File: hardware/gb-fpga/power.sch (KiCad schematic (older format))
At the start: 1 part, among them U1 xc7s25ftgb196

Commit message: Add GND net
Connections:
- net labels added: GND
- wire segments 0 -> 2
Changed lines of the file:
@@
 	1    0    0    -1
 $EndComp
+$Comp
+L power:GND #PWR0102
+U 1 1 60D21807
+P 5500 3700
+F 0 "#PWR0102" H 5500 3450 50  0001 C CNN
+F 1 "GND" H 5505 3527 50  0000 C CNN
+F 2 "" H 5500 3700 50  0001 C CNN
+F 3 "" H 5500 3700 50  0001 C CNN
+	1    5500 3700
+	1    0    0    -1
+$EndComp
+Wire Wire Line
+	6050 3100 5500 3100
+Wire Wire Line
+	5500 3100 5500 3700
 $EndSCHEMATC

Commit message: Connect flash config circuit
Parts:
- removed U1: xc7s25ftgb196, Package_BGA:Xilinx_FTGB196, symbol xilinx7:xc7s25ftgb196
- added U1: xc7s25ftgb196, Package_BGA:Xilinx_FTGB196, symbol gb-fpga:xc7s25ftgb196
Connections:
- net labels added: +1V0, +1V8, +3V3
- wire segments 2 -> 79

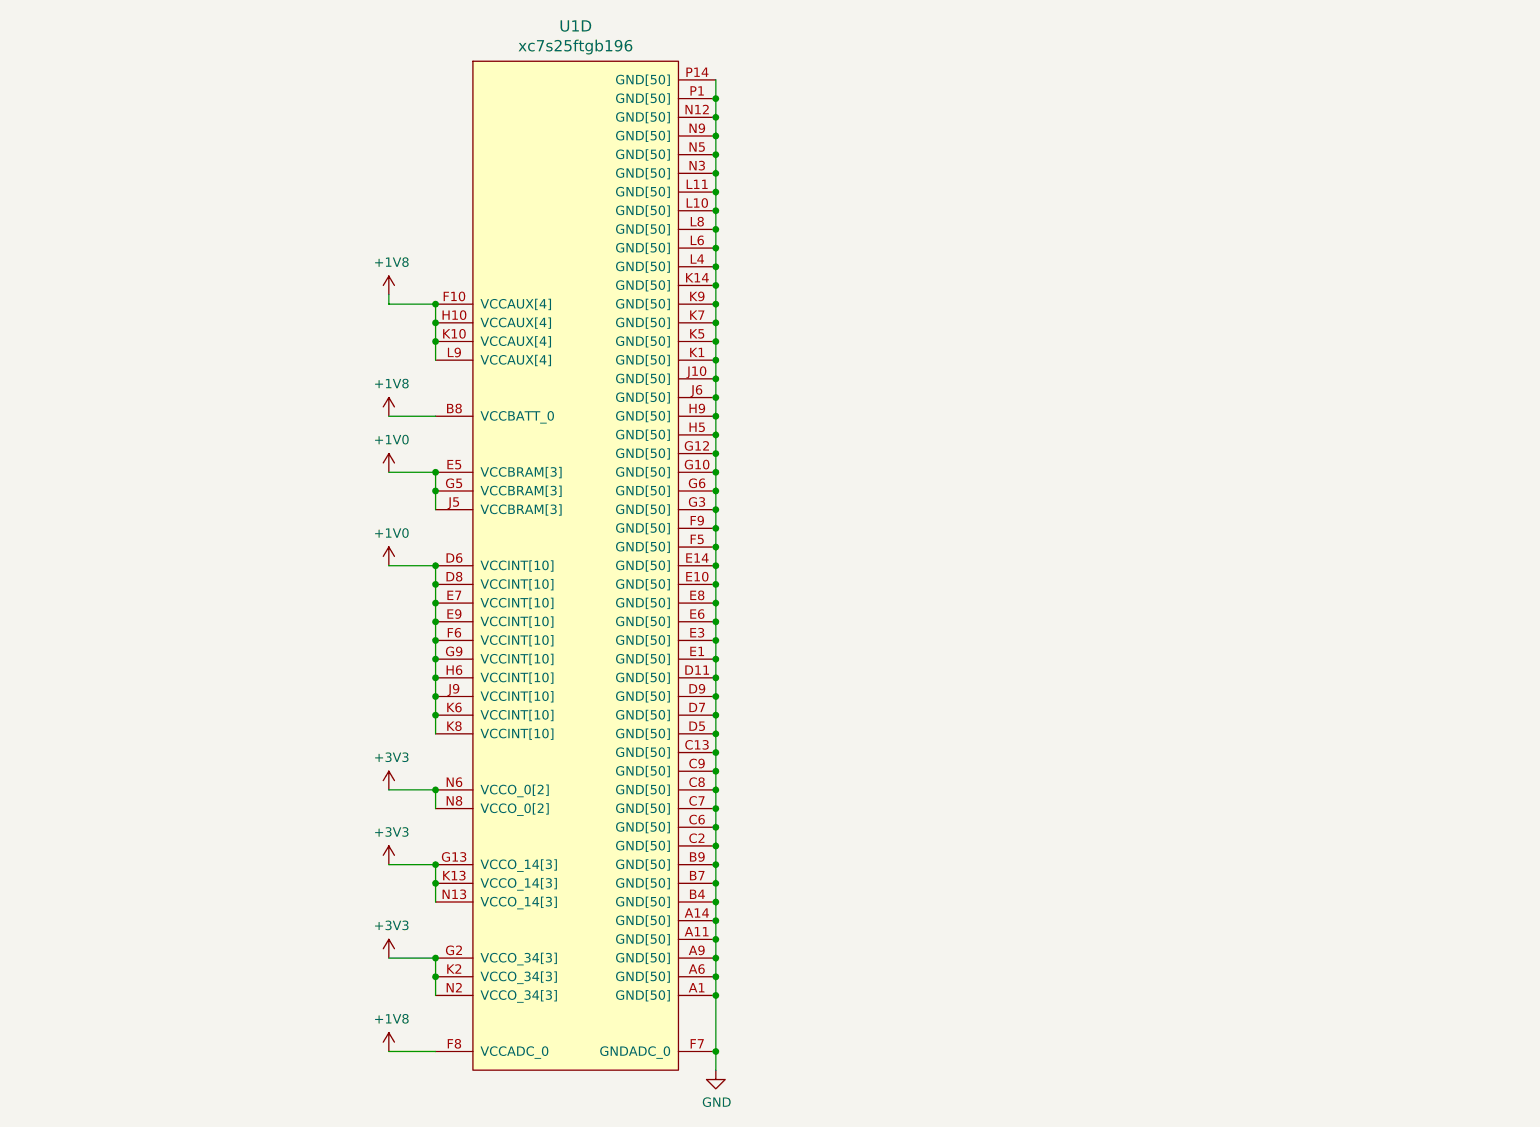
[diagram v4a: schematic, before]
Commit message: Add LTC3555
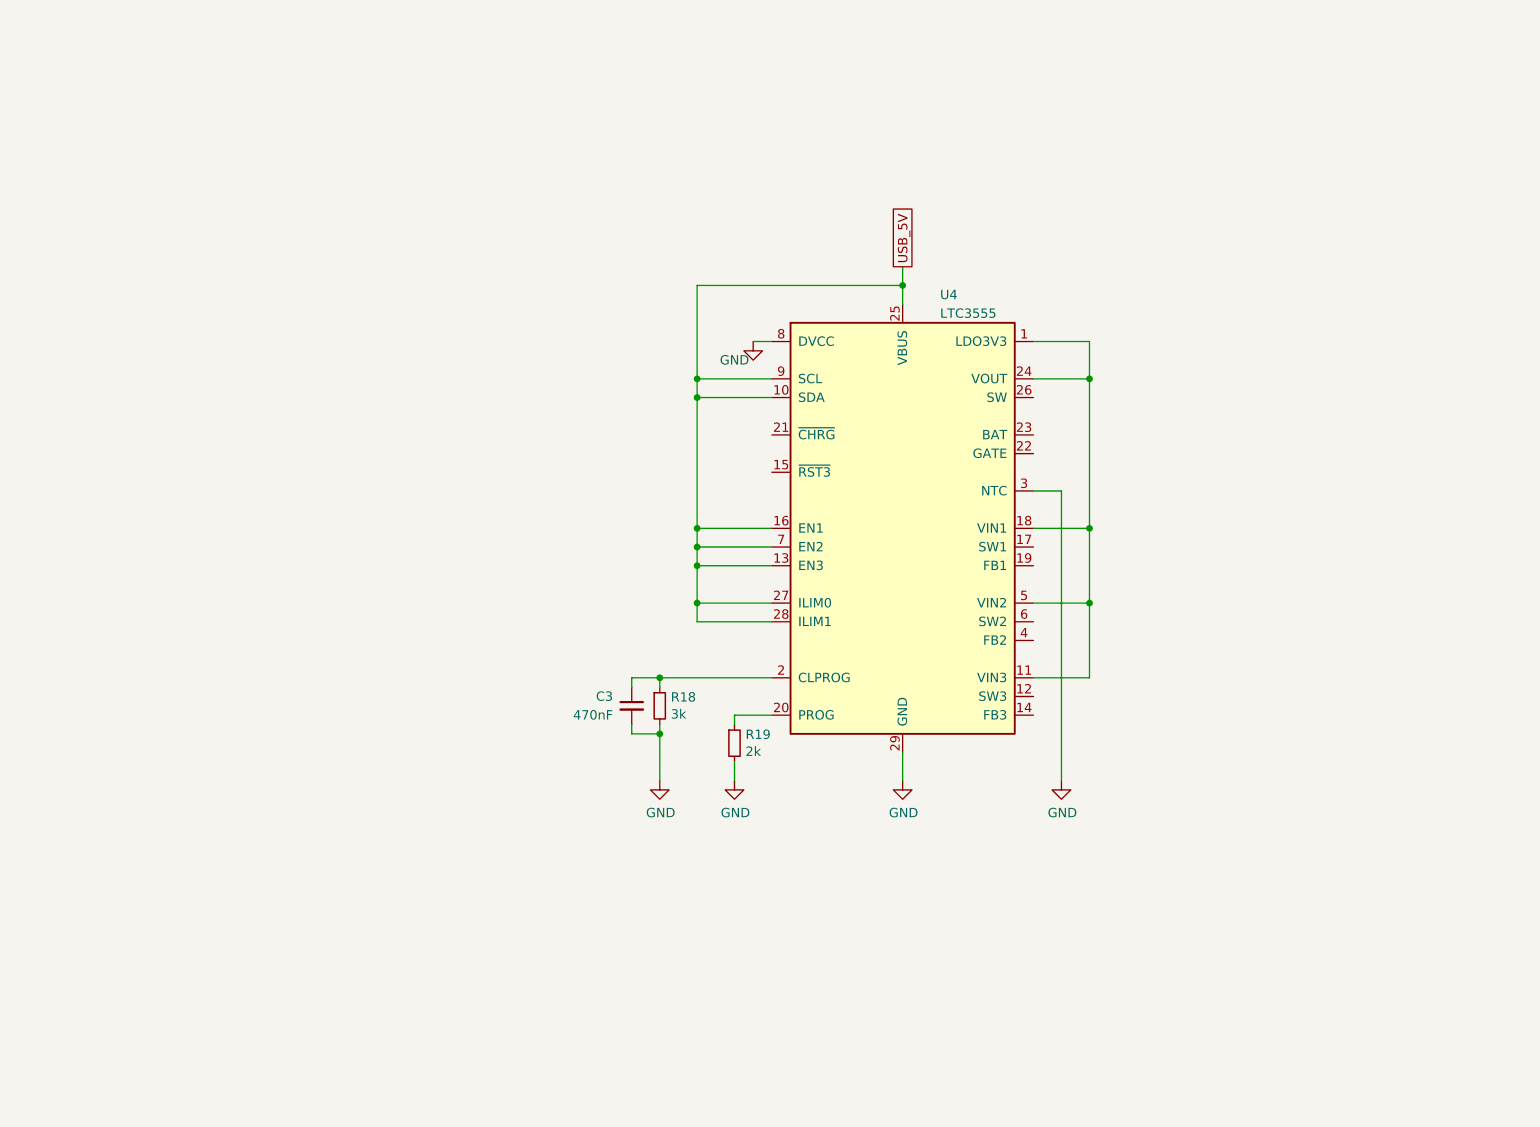
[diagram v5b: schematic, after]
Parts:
- removed U1: xc7s25ftgb196, Package_BGA:Xilinx_FTGB196, symbol gb-fpga:xc7s25ftgb196
- added C3: 470nF, Capacitor_SMD:C_0603_1608Metric, symbol Device:C_Small
- added R18: 3k, Resistor_SMD:R_0603_1608Metric, symbol Device:R_Small
- added R19: 2k, Resistor_SMD:R_0603_1608Metric, symbol Device:R_Small
- added U4: LTC3555, Package_DFN_QFN:QFN-28-1EP_4x5mm_P0.5mm_EP2.65x3.65mm, symbol Battery_Management:LTC3555
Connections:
- net GND: now also C3.2, R18.2, R19.2, U4.29 (GND), U4.3 (NTC), U4.8 (DVCC)
- new net: U4.1 (LDO3V3), U4.11 (VIN3), U4.18 (VIN1), U4.24 (VOUT), U4.5 (VIN2)
- new net: C3.1, R18.1, U4.2 (CLPROG)
- new net: R19.1, U4.20 (PROG)
- new net USB_5V: U4.10 (SDA), U4.13 (EN3), U4.16 (EN1), U4.25 (VBUS), U4.27 (ILIM0), U4.28 (ILIM1), U4.7 (EN2), U4.9 (SCL)

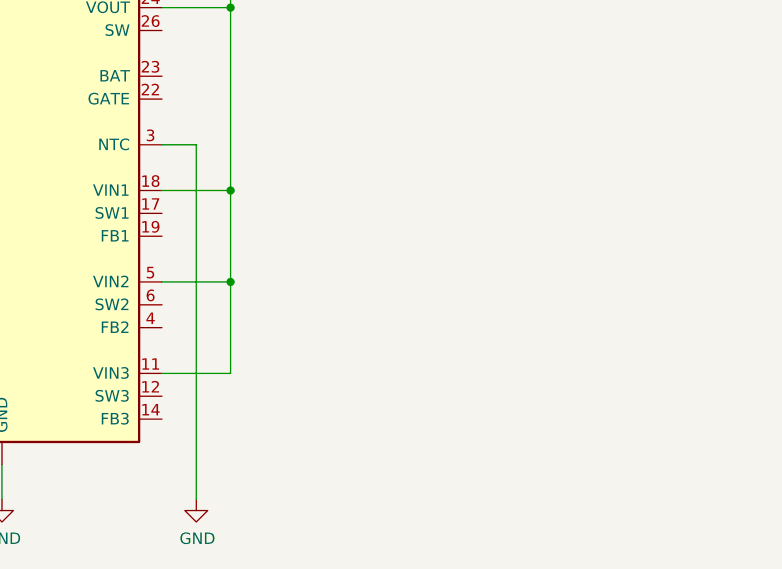
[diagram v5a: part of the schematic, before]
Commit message: Add step-down conversion
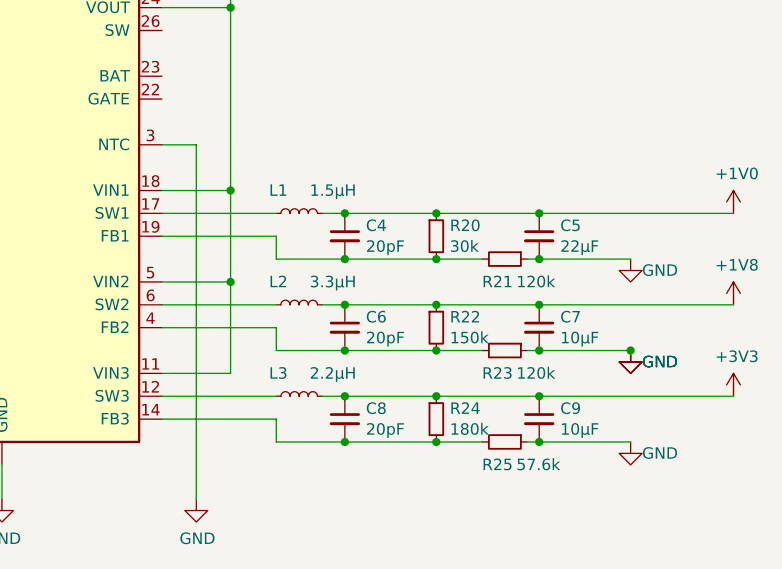
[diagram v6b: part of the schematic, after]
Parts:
- added C4, C6, C8: 20pF, Capacitor_SMD:C_0603_1608Metric, symbol Device:C_Small
- added C5: 22µF, Capacitor_SMD:C_0603_1608Metric, symbol Device:C_Small
- added C7, C9: 10µF, Capacitor_SMD:C_0603_1608Metric, symbol Device:C_Small
- added L1: 1.5µH, Inductor_SMD:L_0603_1608Metric, symbol Device:L_Small
- added L2: 3.3µH, Inductor_SMD:L_0603_1608Metric, symbol Device:L_Small
- added L3: 2.2µH, Inductor_SMD:L_0603_1608Metric, symbol Device:L_Small
- added R20: 30k, Resistor_SMD:R_0603_1608Metric, symbol Device:R_Small
- added R21, R23: 120k, Resistor_SMD:R_0603_1608Metric, symbol Device:R_Small
- added R22: 150k, Resistor_SMD:R_0603_1608Metric, symbol Device:R_Small
- added R24: 180k, Resistor_SMD:R_0603_1608Metric, symbol Device:R_Small
- added R25: 57.6k, Resistor_SMD:R_0603_1608Metric, symbol Device:R_Small
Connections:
- net GND: now also C5.2, C7.2, C9.2, R21.1, R23.1, R25.1
- net at U4.12 (SW3): now also L3.1
- net at U4.14 (FB3): now also C8.2, R24.2, R25.2
- net at U4.17 (SW1): now also L1.1
- net at U4.19 (FB1): now also C4.2, R20.2, R21.2
- net at U4.4 (FB2): now also C6.2, R22.2, R23.2
- net at U4.6 (SW2): now also L2.1
- new net +1V0: C4.1, C5.1, L1.2, R20.1
- new net +1V8: C6.1, C7.1, L2.2, R22.1
- new net +3V3: C8.1, C9.1, L3.2, R24.1

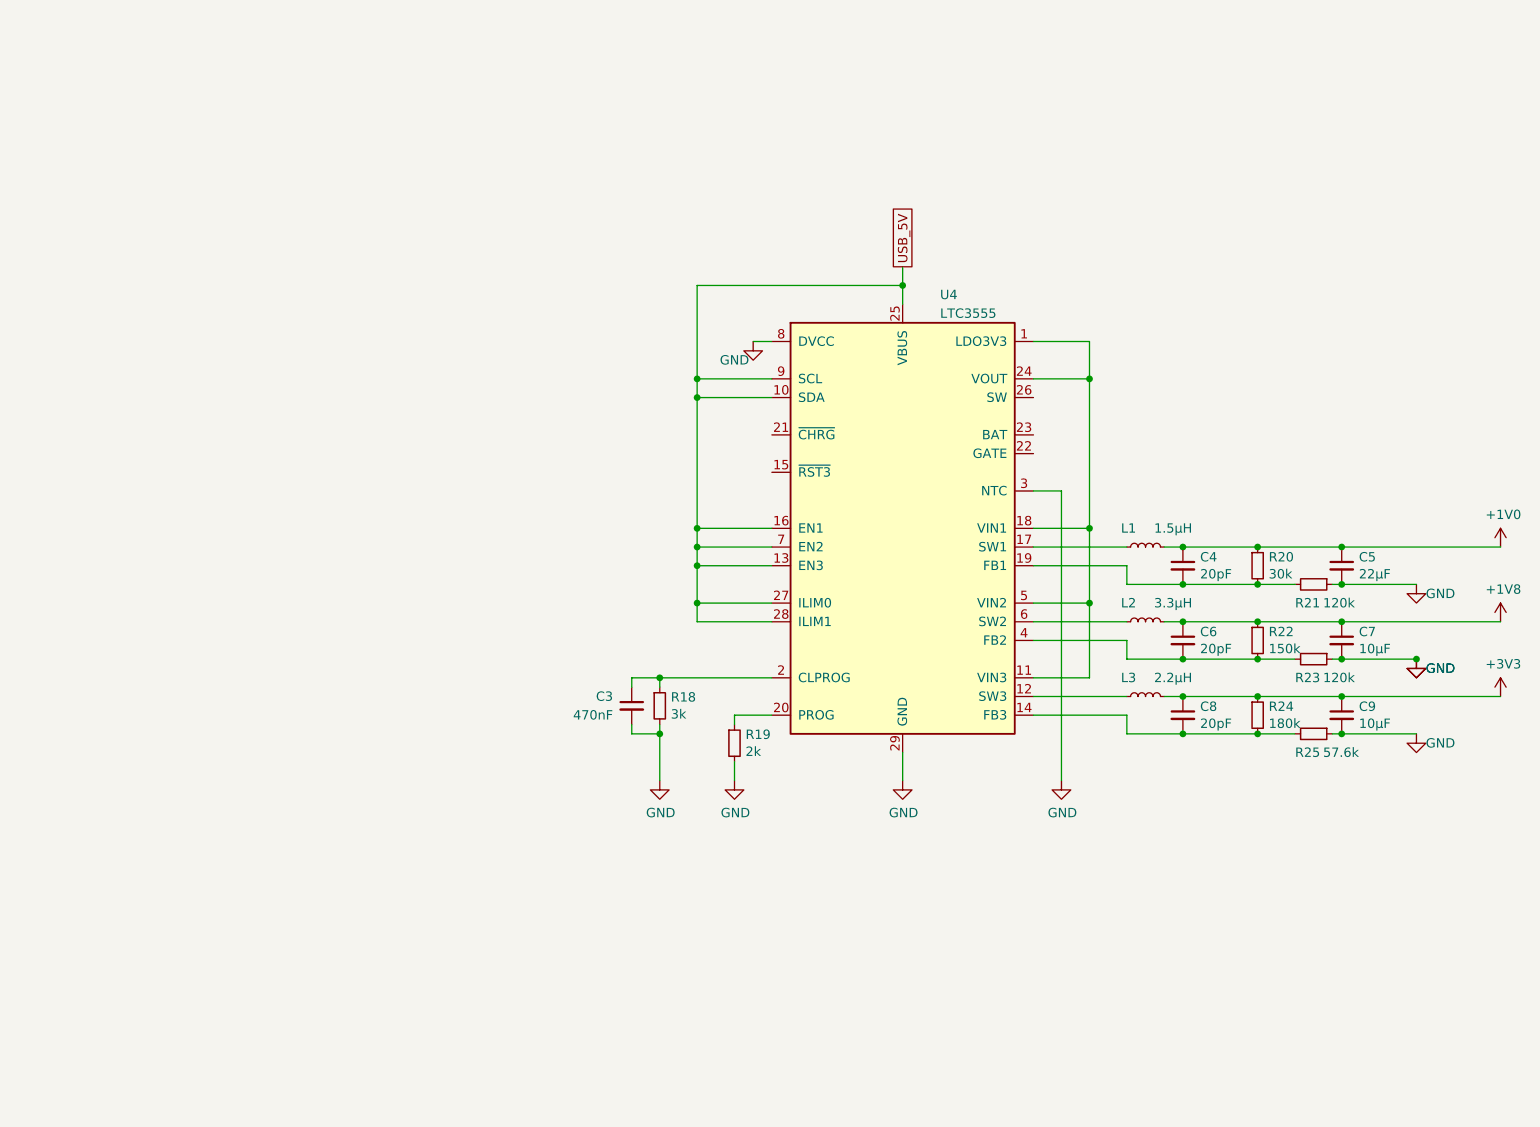
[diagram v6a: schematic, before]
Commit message: Update power circuit
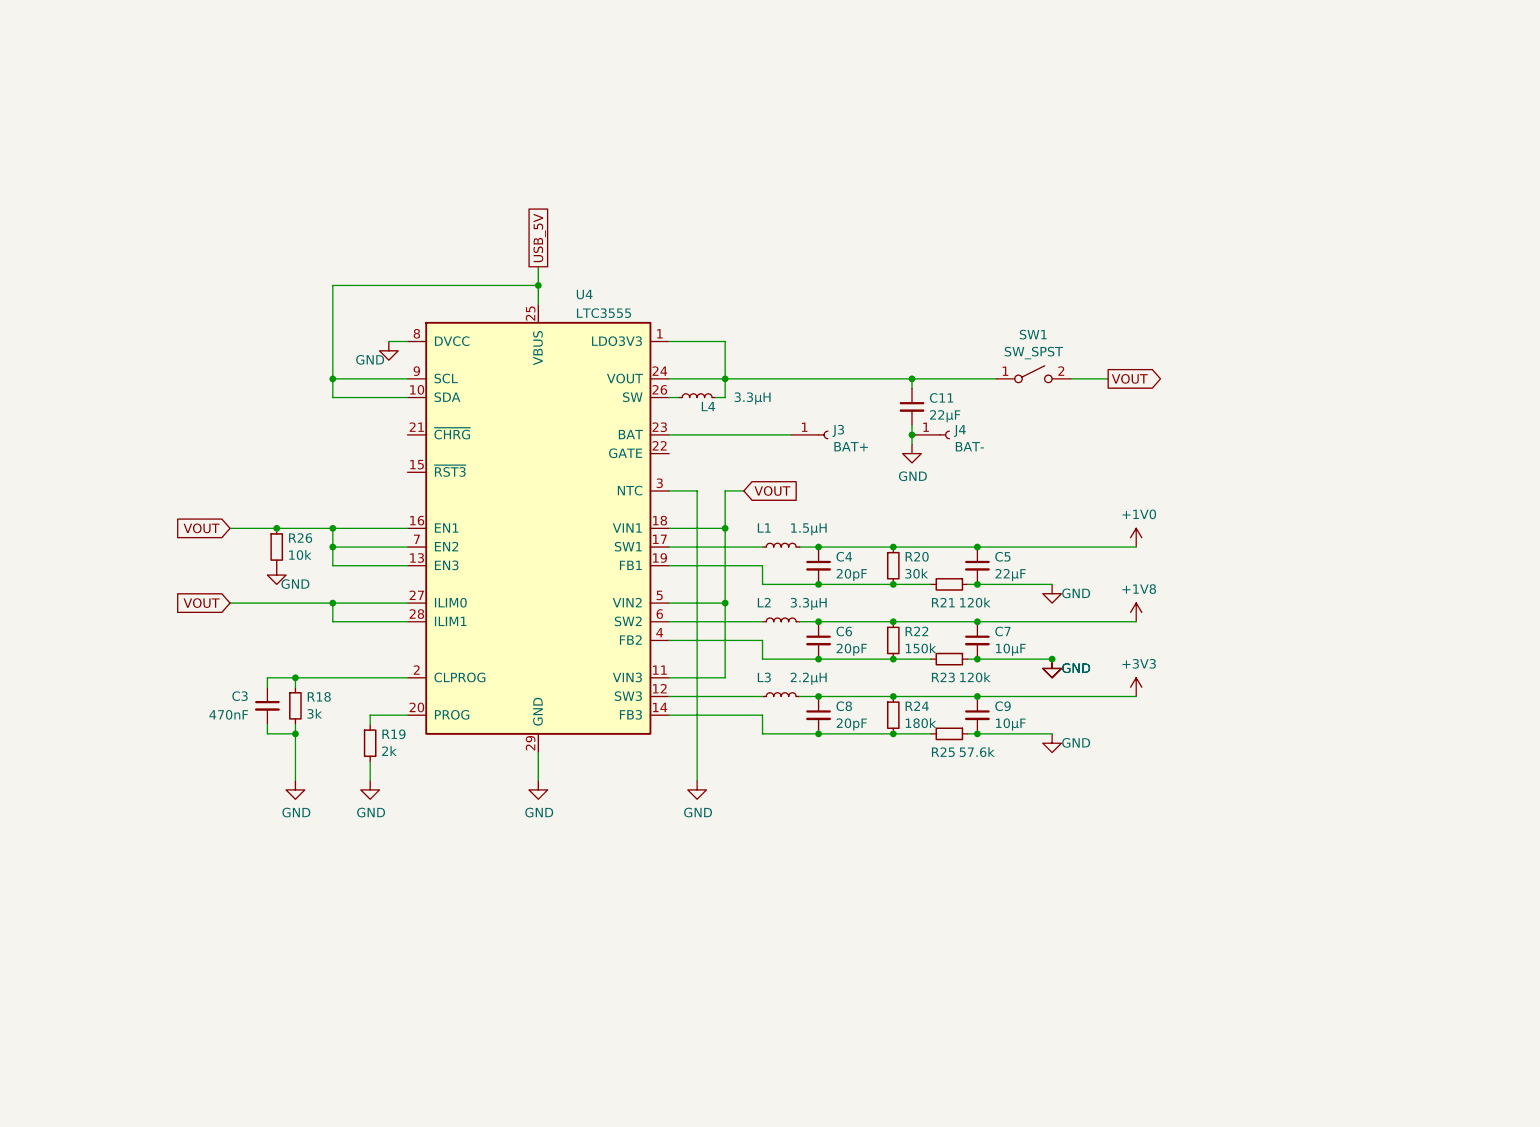
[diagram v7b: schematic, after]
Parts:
- added C11: 22µF, Capacitor_SMD:C_0603_1608Metric, symbol Device:C_Small
- added J3: BAT+, Connector_PinHeader_2.54mm:PinHeader_1x01_P2.54mm_Vertical, symbol Connector:Conn_01x01_Female
- added J4: BAT-, Connector_PinHeader_2.54mm:PinHeader_1x01_P2.54mm_Vertical, symbol Connector:Conn_01x01_Female
- added L4: 3.3µH, Inductor_SMD:L_0603_1608Metric, symbol Device:L_Small
- added R26: 10k, Resistor_SMD:R_0603_1608Metric, symbol Device:R_Small
- added SW1: SW_SPST, symbol Switch:SW_SPST
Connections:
- net GND: now also C11.2, J4.1 (Pin_1), R26.2
- net USB_5V: no longer U4.13 (EN3), U4.16 (EN1), U4.27 (ILIM0), U4.28 (ILIM1), U4.7 (EN2)
- net VOUT: now reaches U4.11 (VIN3), U4.18 (VIN1), U4.5 (VIN2)
- net VOUT: now also U4.13 (EN3), U4.16 (EN1), U4.27 (ILIM0), U4.28 (ILIM1), U4.7 (EN2), R26.1, SW1.2 (B); no longer U4.1 (LDO3V3), U4.24 (VOUT)
- net at U4.23 (BAT): now also J3.1 (Pin_1)
- net at U4.26 (SW): now also L4.1
- new net: C11.1, L4.2, SW1.1 (A), U4.1 (LDO3V3), U4.24 (VOUT)
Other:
- moved on the sheet: C3, C4, C5, C6, C7, C8, C9, L1, L2, L3, R18, R19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
